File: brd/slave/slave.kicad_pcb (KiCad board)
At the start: 2 copper layers, 43.2 x 25.4 mm, 23 parts, among them IC1 ATMEGA328P-A, P1 CONN_3X2, P2 CONN_8, P3 CONN_2, P4 CONN_6, P5 CONN_1, Q1 BC847, U1 LM78L05ACZ, X1 16MHz

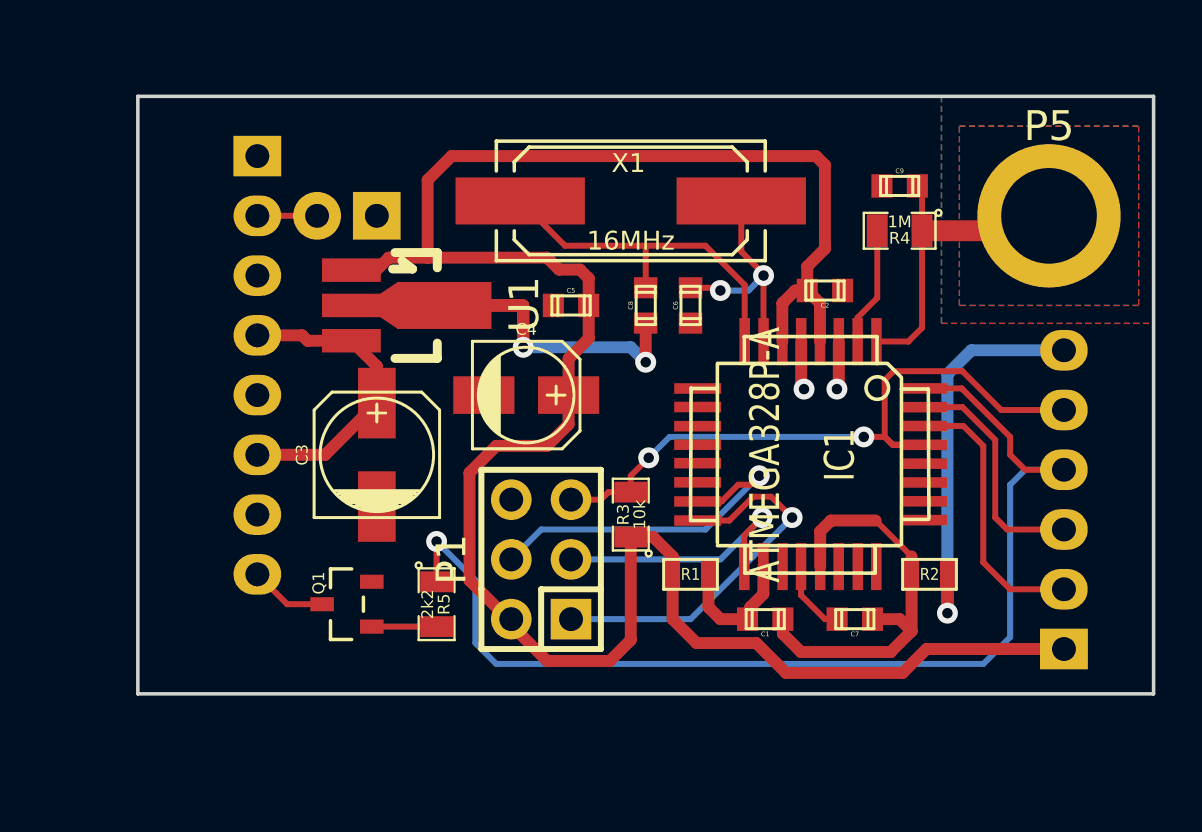
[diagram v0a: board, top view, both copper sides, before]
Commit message: layout rework & gerber generation for slave pcb
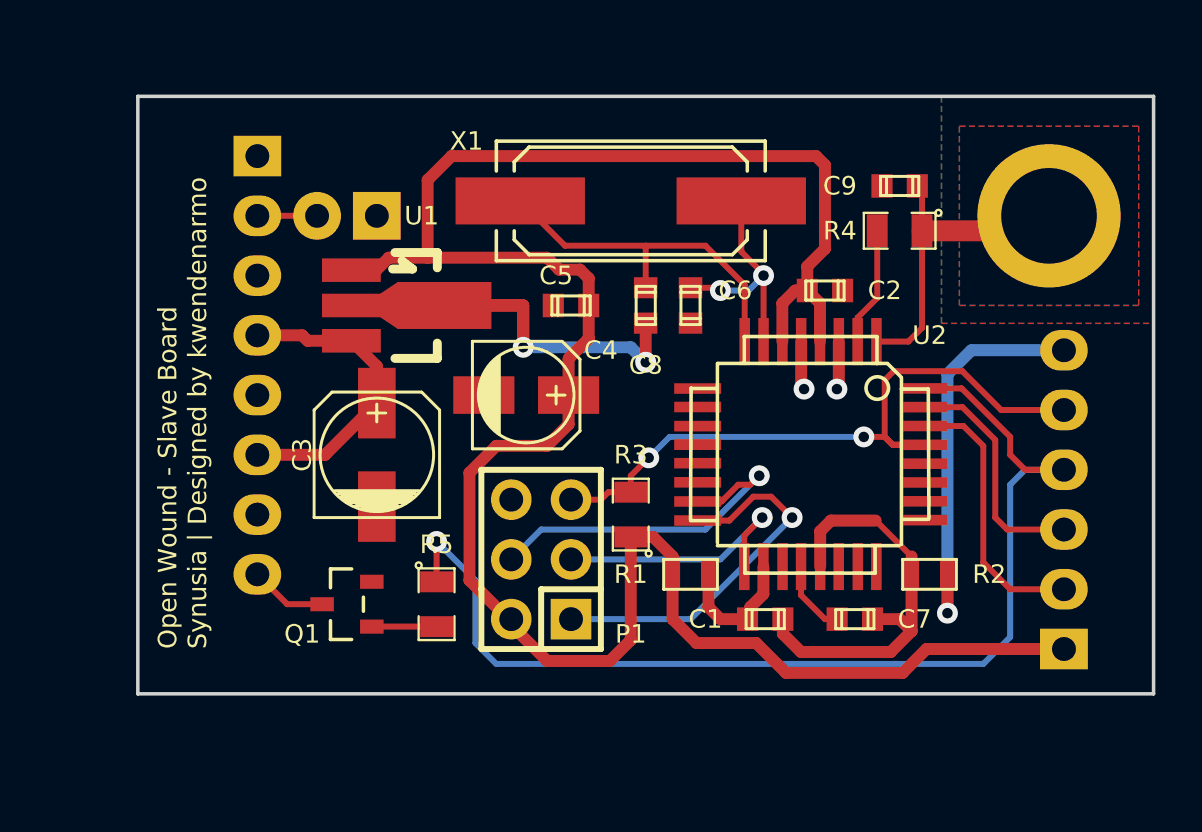
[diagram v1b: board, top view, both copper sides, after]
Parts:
- P2: footprint Pin_Headers:Pin_Header_Angled_1x08 -> Pin_Headers:Pin_Header_Straight_1x08
- P3: footprint Pin_Headers:Pin_Header_Angled_1x02 -> Pin_Headers:Pin_Header_Straight_1x02
- P4: footprint Pin_Headers:Pin_Header_Angled_1x06 -> Pin_Headers:Pin_Header_Straight_1x06
- renumbered IC1 to U2
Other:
- board text added: "Open Wound - Slave Board Synusia | Designed by kwendenarmo"

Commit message: slave version rc3
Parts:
- added REF**: Symbol_OSHW-Logo_SilkScreen, Symbols:Symbol_OSHW-Logo_SilkScreen, B.Cu at (157.5, 103.5)
- C1: value 100nF -> 10uF; footprint Capacitors_SMD:c_0603 -> Capacitors_SMD:c_elec_5x5.3
- C2: value 100nF -> 1uF; footprint Capacitors_SMD:c_0603 -> Capacitors_SMD:c_elec_4x5.3
- C3: value 10uF -> 10nF; footprint Capacitors_SMD:c_elec_5x5.3 -> Capacitors_SMD:C_0603_HandSoldering
- C4: value 1uF -> 100nF; footprint Capacitors_SMD:c_elec_4x5.3 -> Capacitors_SMD:C_0603_HandSoldering
- C5: value 10nF -> 100nF; footprint Capacitors_SMD:c_0603 -> Capacitors_SMD:C_0603_HandSoldering
- C6, C7, C8, C9: footprint Capacitors_SMD:c_0603 -> Capacitors_SMD:C_0603_HandSoldering
- P1: value CONN_3X2 -> AVRISP
- P2: value CONN_8 -> IO; footprint Pin_Headers:Pin_Header_Straight_1x08 -> asrdi-conn:IL-Z-8PL-SMTYE; moved to F.Cu
- P3: value CONN_2 -> PIEZO; footprint Pin_Headers:Pin_Header_Straight_1x02 -> asrdi-conn:IL-Z-2PL-SMTYE; moved to F.Cu
- P4: value CONN_6 -> DEBUG; footprint Pin_Headers:Pin_Header_Straight_1x06 -> asrdi-conn:IL-Z-6PL-SMTYE; moved to F.Cu
- P5: value CONN_1 -> SENSE
- Q1: footprint Transistors_SMD:sot23 -> Housings_SOT-23_SOT-143_TSOT-6:SOT-23_Handsoldering
- R1, R2: footprint SMD_Packages:SM0603 -> Resistors_SMD:R_0603_HandSoldering
- R3, R4, R5: footprint SMD_Packages:SM0805 -> Resistors_SMD:R_0805_HandSoldering
- U2: footprint SMD_Packages:TQFP32 -> Housings_QFP:TQFP-32_7x7mm_Pitch0.8mm
- moved C5 19.1 mm to (151.1, 114.3)
- moved C1 18.7 mm to (139.1, 105.4), turned to 90 degrees
- moved C4 17.3 mm to (157.5, 113.0)
- moved C2 15.9 mm to (146.1, 102.2), turned to 0 degrees
- moved P2 13.0 mm to (133.3, 110.5), turned to 180 degrees
- moved P3 7.75 mm to (133.3, 95.9), turned to 90 degrees
- moved R2 6.63 mm to (162.6, 113.0)
- moved P1 6.48 mm to (146.7, 112.4), turned to 180 degrees
- moved Q1 6.35 mm to (135.9, 113.0)
- moved C3 6.25 mm to (146.7, 99.1), turned to 180 degrees
- moved R5 5.46 mm to (140.3, 112.4)
- moved R3 5.43 mm to (149.9, 109.2)
- moved R4 4.96 mm to (159.4, 95.2), turned to 270 degrees
- moved R1 4.84 mm to (152.4, 111.1), turned to 270 degrees
- moved P4 4.49 mm to (165.7, 104.1), turned to 0 degrees
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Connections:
- C1 pad 1: +5VA -> VCC
- C1 pad 2: AGND -> GND
- C3 pad 1: VCC -> +5V
- C4 pad 1: +5V -> +5VA
- C4 pad 2: GND -> GNDA
- C7 pad 2: AGND -> GNDA
- R2 pad 2: AGND -> GNDA
- R5 pad 1: Net-(P4-Pad4) -> Net-(P4-Pad2)
- U2 pad 21: AGND -> GNDA
- U2 pad 30: Net-(P4-Pad2) -> Net-(P4-Pad4)
- U2 pad 32: Net-(P4-Pad4) -> Net-(P4-Pad2)
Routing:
- net Net-(P4-Pad2): track 11.7 -> 53.9 mm, vias 0 -> 3
- net Net-(P4-Pad4): track 47.2 -> 19.3 mm, vias 1 -> 2
- net GND: track 38.9 -> 12.5 mm
- net Net-(P2-Pad2): track 2.54 -> 25.1 mm, vias 0 -> 2
- net AGND: track 18.0 -> 0.00 mm
- net Net-(P1-Pad5): track 29.3 -> 45.4 mm
- net Net-(P2-Pad8): track 3.28 -> 19.1 mm
- net Net-(P4-Pad3): track 10.1 -> 19.6 mm, vias 0 -> 2
- net GNDA: track 0.00 -> 8.53 mm
- net +5V: track 94.6 -> 88.1 mm, vias 0 -> 4
- net Net-(P1-Pad4): track 15.1 -> 21.0 mm
- net +5VA: track 5.78 -> 11.6 mm
- net VCC: track 13.2 -> 17.4 mm
- net Net-(P1-Pad3): track 11.3 -> 15.2 mm, vias 1 -> 0
- net Net-(C6-Pad1): track 9.79 -> 6.66 mm, vias 2 -> 0
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- removed copper zone on B.Cu, net Net-(C9-Pad1)
- removed copper zone on F.Cu, net Net-(C9-Pad1)
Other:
- board size 43.2 x 25.4 mm -> 45.1 x 26 mm
- net class Default: clearance 0.254 -> 0.2032; via_dia 0.889 -> 0.59944; via_drill 0.635 -> 0.39878
- net class Power: clearance 0.254 -> 0.2032; via_dia 0.889 -> 0.59944; via_drill 0.635 -> 0.39878
- net class Sense removed
- rule trace_clearance: 0.254 -> 0.2032
- rule trace_min: 0.254 -> 0.2032
- rule via_min_drill: 0.508 -> 0.29972
- rule via_min_size: 0.889 -> 0.39878
- board text added: "Open Wound - Slave board rc3 Synusia | Designed by kwendenarmo https://github.com/synusia/open-wound UNDER MIT LICENSE"
- board text removed: "Open Wound - Slave Board Synusia | Designed by kwendenarmo"

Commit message: versión 1.0.0
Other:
- board text added: "Open Wound - Slave board 1.0.0 Synusia | Designed by kwendenarmo https://github.com/synusia/open-wound UNDER GPLv3 LICENSE"
- board text removed: "Open Wound - Slave board rc3 Synusia | Designed by kwendenarmo https://github.com/synusia/open-wound UNDER MIT LICENSE"
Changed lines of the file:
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@@
-(kicad_pcb (version 4) (host pcbnew 0.201505222246+5678~23~ubuntu14.04.1-product)
+(kicad_pcb (version 4) (host pcbnew 0.201506282246+5838~23~ubuntu14.04.1-product)
   (general
     (links 59)
@@
     (32 B.Adhes user hide)
     (33 F.Adhes user hide)
-    (34 B.Paste user hide)
+    (34 B.Paste user)
     (35 F.Paste user hide)
     (36 B.SilkS user)
-    (37 F.SilkS user hide)
-    (38 B.Mask user hide)
-    (39 F.Mask user hide)
+    (37 F.SilkS user)
+    (38 B.Mask user)
+    (39 F.Mask user)
     (40 Dwgs.User user hide)
     (41 Cmts.User user hide)
@@
     (pad_to_mask_clearance 0)
     (aux_axis_origin 0 0)
-    (visible_elements FFFEBF5F)
+    (visible_elements FFFEFF5F)
     (pcbplotparams
       (layerselection 0x00010_00000000)
@@
     (fp_line (start 0.35052 -0.89916) (end 0.7493 -1.89992) (layer B.SilkS) (width 0.15))
   )
-  (gr_text "Open Wound - Slave board rc3\nSynusia | Designed by kwendenarmo\n\nhttps://github.com/synusia/open-wound\n\nUNDER MIT LICENSE" (at 160.655 95.25) (layer B.SilkS)
+  (gr_text "Open Wound - Slave board 1.0.0\nSynusia | Designed by kwendenarmo\n\nhttps://github.com/synusia/open-wound\n\nUNDER GPLv3 LICENSE" (at 161.925 95.25) (layer B.SilkS)
     (effects (font (size 1.016 1.016) (thickness 0.1524)) (justify left mirror))
   )
